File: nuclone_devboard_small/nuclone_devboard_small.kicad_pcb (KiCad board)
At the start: 2 copper layers, 48.3 x 48.3 mm, 57 parts, among them J1 JTAG_2X05, J2 USB-ID, J3 nuclone_20pin_gpio, J4 nuclone_20pin_bus_analog, U1 USBLC6-2, U2 MCP1702-MB, U3 LPC812M101JDH20, Y1 12MHz

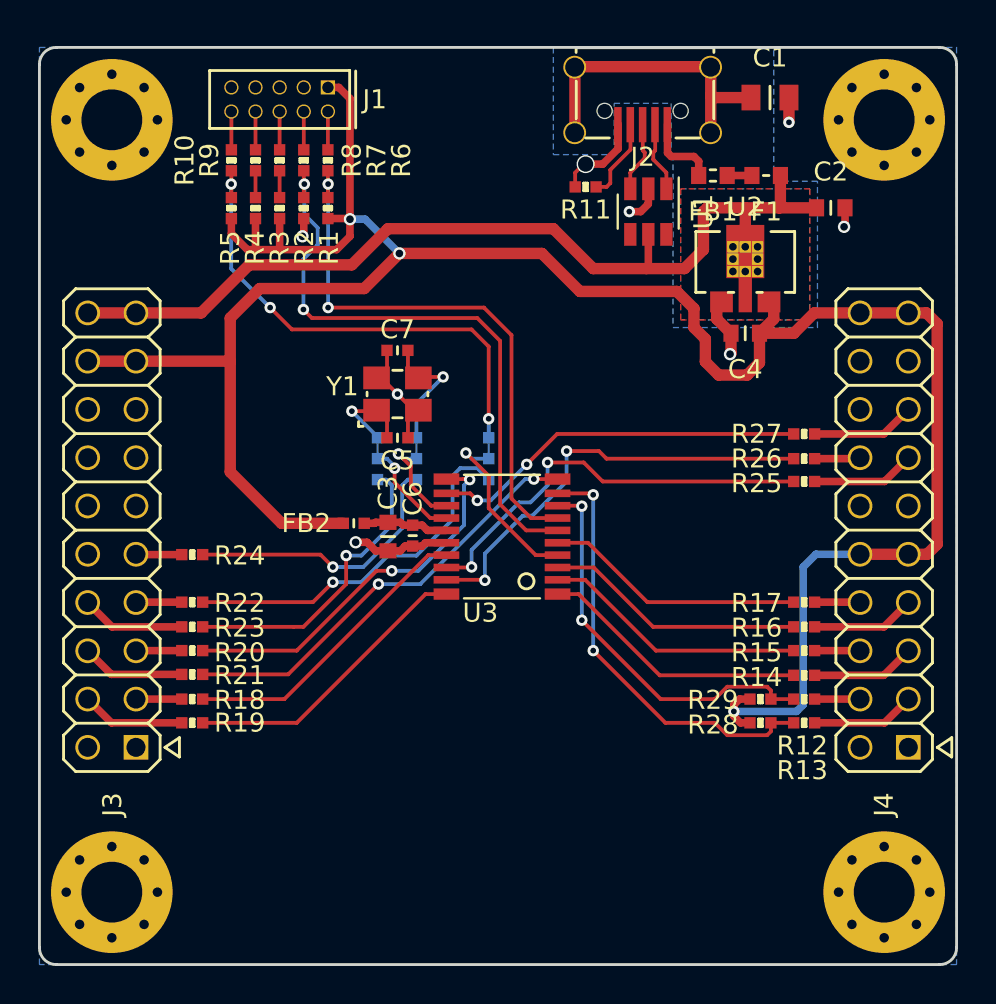
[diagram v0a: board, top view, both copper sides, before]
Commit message: initial component placement
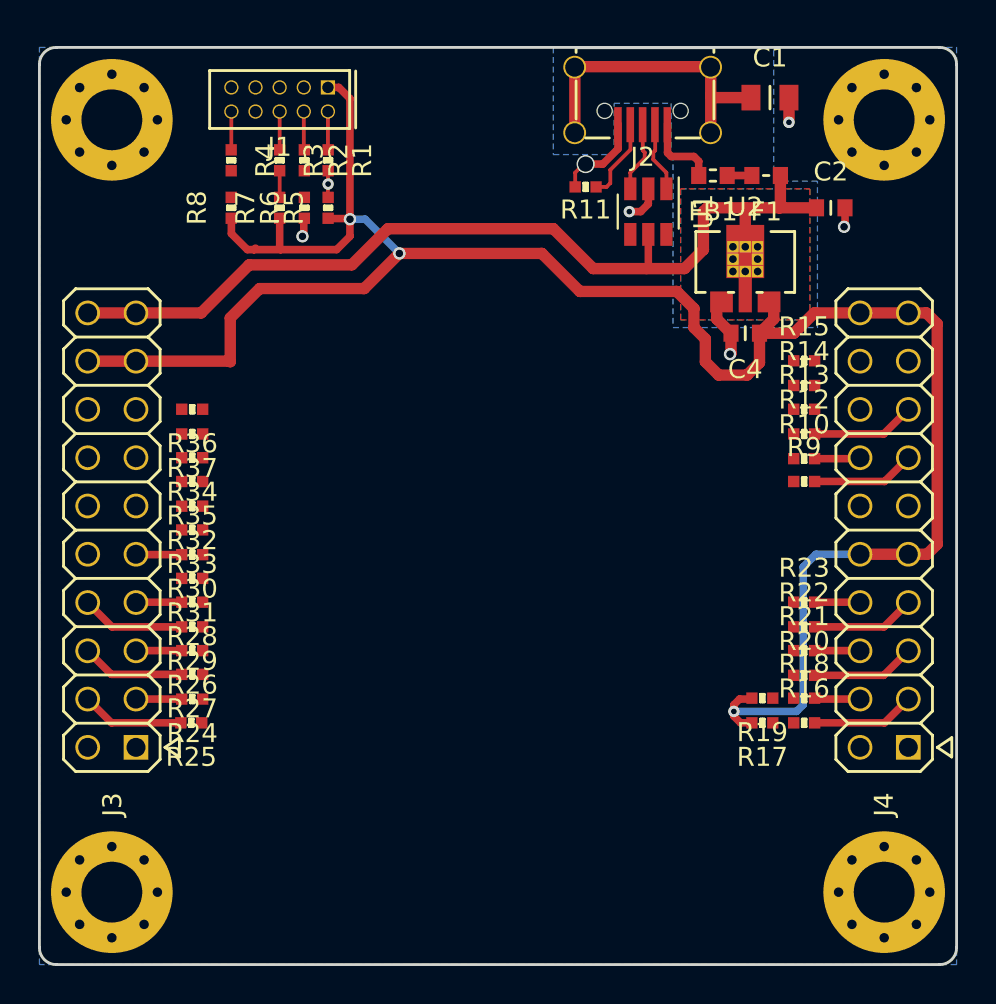
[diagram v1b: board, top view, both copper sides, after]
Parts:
- removed C3: 10u, SquantorRcl:C_0603
- removed C5, C7: 18p, SquantorRcl:C_0402
- removed C6: 1u, SquantorRcl:C_0402
- removed FB2: FB, SquantorRcl:C_0402
- removed JP1: RESET/GPIO_04, SquantorSpecial:solder_jumper_3way_23conn
- removed JP2: XTAL/GPIO_05, SquantorSpecial:solder_jumper_3way_23conn
- removed JP3: XTAL/GPIO_06, SquantorSpecial:solder_jumper_3way_23conn
- removed U3: LPC812M101JDH20, SquantorIC:SOT360
- removed Y1: 12MHz, SquantorCrystal:Crystal_3225_4
- added R30: 100, SquantorRcl:R_0402_hand, F.Cu at (69.0, 87.7)
- added R31: 100, SquantorRcl:R_0402_hand, F.Cu at (69.0, 88.9)
- added R32: 100, SquantorRcl:R_0402_hand, F.Cu at (69.0, 85.1)
- added R33: 100, SquantorRcl:R_0402_hand, F.Cu at (69.0, 86.3)
- added R34: 100, SquantorRcl:R_0402_hand, F.Cu at (69.0, 82.5)
- added R35: 100, SquantorRcl:R_0402_hand, F.Cu at (69.0, 83.8)
- added R36: 100, SquantorRcl:R_0402_hand, F.Cu at (69.0, 80.0)
- added R37: 100, SquantorRcl:R_0402_hand, F.Cu at (69.0, 81.3)
- R1, R4: value 100K -> 100
- R17, R19: value 100 -> 2.2K
- R2, R3: value 100k -> 100
- R28, R29: value 2.2K -> 100
- R5: value 100k -> 100K
- R6, R7, R8: value 100 -> 100k
- moved R25 34.7 mm to (69.0, 96.5), turned to 180 degrees
- moved R27 34.6 mm to (69.0, 94.0), turned to 180 degrees
- moved R10 34.0 mm to (101.2, 82.6), turned to 0 degrees
- moved R26 33.7 mm to (69.0, 92.7), turned to 180 degrees
- moved R9 33.5 mm to (101.2, 83.8), turned to 0 degrees
- moved R20 32.2 mm to (101.2, 94.0), turned to 0 degrees
- moved R22 32.2 mm to (101.2, 91.5), turned to 0 degrees
- moved R23 32.2 mm to (101.2, 90.2), turned to 0 degrees
- moved R21 32.2 mm to (101.2, 92.7), turned to 0 degrees
- moved R18 32.2 mm to (101.2, 95.2), turned to 0 degrees
- moved R28 30.6 mm to (69.0, 90.2), turned to 180 degrees
- moved R29 30.1 mm to (69.0, 91.5), turned to 180 degrees
- moved R19 30.0 mm to (99.0, 95.2)
- moved R13 15.2 mm to (101.2, 80.0)
- moved R14 15.2 mm to (101.2, 78.8)
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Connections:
- C1 pad 2: VSS -> /VSS
- C2 pad 2: VSS -> /VSS
- C4 pad 2: VSS -> /VSS
- J1 pad 3: VSS -> /VSS
- J1 pad 5: VSS -> /VSS
- J1 pad 8: Net-(J1-Pad8) -> (no net)
- J1 pad 9: VSS -> /VSS
- J2 pad 5: VSS -> /VSS
- J3 pad 1: VSS -> /VSS
- J3 pad 10: (no net) -> /GPIO_07
- J3 pad 11: (no net) -> /GPIO_08
- J3 pad 12: (no net) -> /GPIO_09
- J3 pad 13: (no net) -> /GPIO_10
- J3 pad 14: (no net) -> /GPIO_11
- J3 pad 15: (no net) -> /GPIO_12
- J3 pad 16: (no net) -> /GPIO_13
- J3 pad 2: VSS -> /VSS
- J4 pad 1: VSS -> /VSS
- J4 pad 11: VSS -> /VSS
- J4 pad 12: VSS -> /VSS
- J4 pad 16: (no net) -> /AN_02
- J4 pad 17: (no net) -> /AN_03
- J4 pad 18: (no net) -> /AN_04
- J4 pad 2: VSS -> /VSS
- R1 pad 1: /VDD -> Net-(J1-Pad2)
- R1 pad 2: /MCU_TMS -> /TMS
- R10 pad 1: Net-(J1-Pad10) -> (no net)
- R10 pad 2: /MCU_RESET -> /AN_00
- R11 pad 1: VSS -> /VSS
- R12 pad 1: /LPC812M101JD20 base/PIO0_10 -> (no net)
- R12 pad 2: /I2C_SDA -> /AN_01
- R13 pad 1: /LPC812M101JD20 base/PIO0_11 -> (no net)
- R13 pad 2: /I2C_SCL -> /AN_02
- R14 pad 1: /LPC812M101JD20 base/PIO0_17 -> (no net)
- R14 pad 2: /SPI_MOSI -> /AN_03
- R15 pad 1: /LPC812M101JD20 base/PIO0_13 -> (no net)
- R15 pad 2: /SPI_MISO -> /AN_04
- R16 pad 1: /LPC812M101JD20 base/PIO0_12 -> /I2C_SDA_INT
- R16 pad 2: /SPI_SCLK -> /I2C_SDA
- R17 pad 1: /LPC812M101JD20 base/PIO0_4 -> /I2C_SDA_INT
- R17 pad 2: /SPI_CE -> /VDD
- R18 pad 1: /LPC812M101JD20 base/PIO0_7 -> /I2C_SCL_INT
- R18 pad 2: /GPIO_00 -> /I2C_SCL
- R19 pad 1: /LPC812M101JD20 base/PIO0_14 -> /I2C_SCL_INT
- R19 pad 2: /GPIO_01 -> /VDD
- R2 pad 1: VSS -> Net-(J1-Pad4)
- R2 pad 2: /MCU_TCK -> /TCK
- R20 pad 1: /LPC812M101JD20 base/PIO0_15 -> (no net)
- R20 pad 2: /GPIO_02 -> /SPI_MOSI
- R21 pad 1: /LPC812M101JD20 base/PIO0_16 -> (no net)
- R21 pad 2: /GPIO_03 -> /SPI_MISO
- R22 pad 1: /LPC812M101JD20 base/GPIO_04_INT -> (no net)
- R22 pad 2: /GPIO_04 -> /SPI_SCLK
- R23 pad 1: /LPC812M101JD20 base/GPIO_05_INT -> (no net)
- R23 pad 2: /GPIO_05 -> /SPI_CE
- R24 pad 1: /LPC812M101JD20 base/GPIO_06_INT -> (no net)
- R24 pad 2: /GPIO_06 -> /GPIO_00
- R25 pad 1: /LPC812M101JD20 base/PIO0_6 -> (no net)
- R25 pad 2: /VREF -> /GPIO_01
- R26 pad 1: /LPC812M101JD20 base/PIO0_0 -> (no net)
- R26 pad 2: /AN_00 -> /GPIO_02
- R27 pad 1: /LPC812M101JD20 base/PIO0_1 -> (no net)
- R27 pad 2: /AN_01 -> /GPIO_03
- R28 pad 1: /VDD -> (no net)
- R28 pad 2: /LPC812M101JD20 base/PIO0_10 -> /GPIO_04
- R29 pad 1: /VDD -> (no net)
- R29 pad 2: /LPC812M101JD20 base/PIO0_11 -> /GPIO_05
- R3 pad 1: /VDD -> Net-(J1-Pad6)
- R3 pad 2: /MCU_TDO -> /TDO
- R4 pad 1: /VDD -> Net-(J1-Pad10)
- R4 pad 2: /Jtag connector/TDI -> /RESET
- R5 pad 2: /MCU_RESET -> /TMS
- R6 pad 1: Net-(J1-Pad2) -> /VSS
- R6 pad 2: /MCU_TMS -> /TCK
- R7 pad 1: Net-(J1-Pad4) -> /VDD
- R7 pad 2: /MCU_TCK -> /TDO
- R8 pad 1: Net-(J1-Pad6) -> /VDD
- R8 pad 2: /MCU_TDO -> /RESET
- R9 pad 1: Net-(J1-Pad8) -> (no net)
- R9 pad 2: /Jtag connector/TDI -> /VREF
- U1 pad 2: VSS -> /VSS
- U2 pad 1: VSS -> /VSS
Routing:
- net /MCU_TCK: track 31.9 -> 0.00 mm, vias 2 -> 0
- net /MCU_TMS: track 29.6 -> 0.00 mm, vias 2 -> 0
- net /MCU_RESET: track 25.9 -> 0.00 mm, vias 3 -> 0
- net VSS: track 24.5 -> 0.00 mm, vias 8 -> 0
- net /LPC812M101JD20 base/PIO0_10: track 23.0 -> 0.00 mm, vias 2 -> 0
- net /LPC812M101JD20 base/PIO0_0: track 23.0 -> 0.00 mm, vias 2 -> 0
- net /LPC812M101JD20 base/PIO0_16: track 22.9 -> 0.00 mm, vias 2 -> 0
- net /LPC812M101JD20 base/PIO0_6: track 22.2 -> 0.00 mm, vias 2 -> 0
- net /LPC812M101JD20 base/PIO0_11: track 21.0 -> 0.00 mm, vias 2 -> 0
- net /LPC812M101JD20 base/PIO0_15: track 20.3 -> 0.00 mm, vias 2 -> 0
- net /LPC812M101JD20 base/PIO0_1: track 19.9 -> 0.00 mm, vias 2 -> 0
- net /LPC812M101JD20 base/GPIO_04_INT: track 19.6 -> 0.00 mm, vias 1 -> 0
- net /LPC812M101JD20 base/GPIO_05_INT: track 16.0 -> 0.00 mm, vias 1 -> 0
- net /LPC812M101JD20 base/PIO0_7: track 16.0 -> 0.00 mm
- net /LPC812M101JD20 base/PIO0_14: track 15.6 -> 0.00 mm
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- added copper zone on B.Cu, net /VSS
- removed copper zone on B.Cu, net VSS

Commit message: routing and silk placement completed, optimized placement and routing a bit
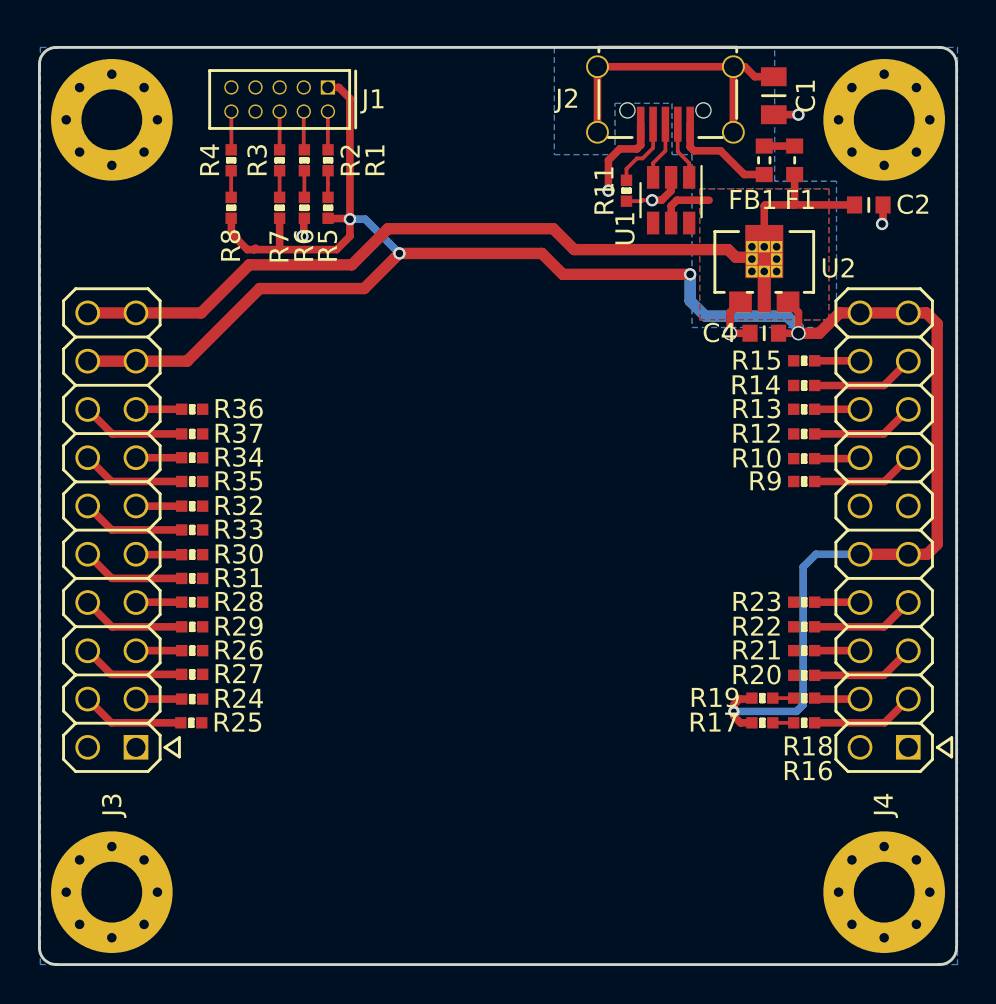
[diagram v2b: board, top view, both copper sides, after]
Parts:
- moved FB1 2.82 mm to (99.1, 66.9), turned to 270 degrees
- moved R11 2.16 mm to (91.8, 68.5), turned to 90 degrees
- moved C2 2.01 mm to (104.6, 69.2)
- moved F1 1.70 mm to (100.7, 66.9), turned to 90 degrees
- moved U1 1.34 mm to (94.2, 69.0)
- moved J2 1.20 mm to (93.9, 63.7)
- moved C4 1.00 mm to (99.1, 76.0)
- moved U2 1.00 mm to (99.1, 72.6)
- moved C1 0.22 mm to (99.6, 63.5), turned to 270 degrees
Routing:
- net /GPIO_13: track 0.00 -> 5.48 mm
- net /GPIO_07: track 0.00 -> 5.48 mm
- net /GPIO_09: track 0.00 -> 5.47 mm
- net /GPIO_11: track 0.00 -> 5.47 mm
- net /AN_03: track 0.00 -> 5.46 mm
- net /VDD: track 112.1 -> 108.5 mm, vias 3 -> 5
- net /GPIO_12: track 0.00 -> 2.41 mm
- net /GPIO_08: track 0.00 -> 2.41 mm
- net /GPIO_10: track 0.00 -> 2.41 mm
- net /AN_04: track 0.00 -> 2.40 mm
- net /AN_02: track 0.00 -> 2.39 mm
- net /VBUS: track 52.2 -> 49.9 mm
- net Net-(FB1-Pad2): track 4.08 -> 5.70 mm
- net /TCK: track 0.00 -> 1.40 mm
- net /RESET: track 0.00 -> 1.40 mm
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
